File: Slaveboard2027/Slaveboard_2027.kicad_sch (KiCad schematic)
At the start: 137 parts, among them J1 Conn_01x01, J10 PB MB, J11 PA MA, J2 Conn_01x01, J3 Conn_01x01, J4 Conn_01x01, J5 Cells, J6 Temp, J7 Temp, J8 Temp, J9 Temp, Q1 DZTT5551, U1 LTC6812, U2 ADG728, U3 ADG728, U4 ADG728, U5 ADG728, U6 LTC6255, U7 LTC6255, U8 LTC6255, U9 LTC6255

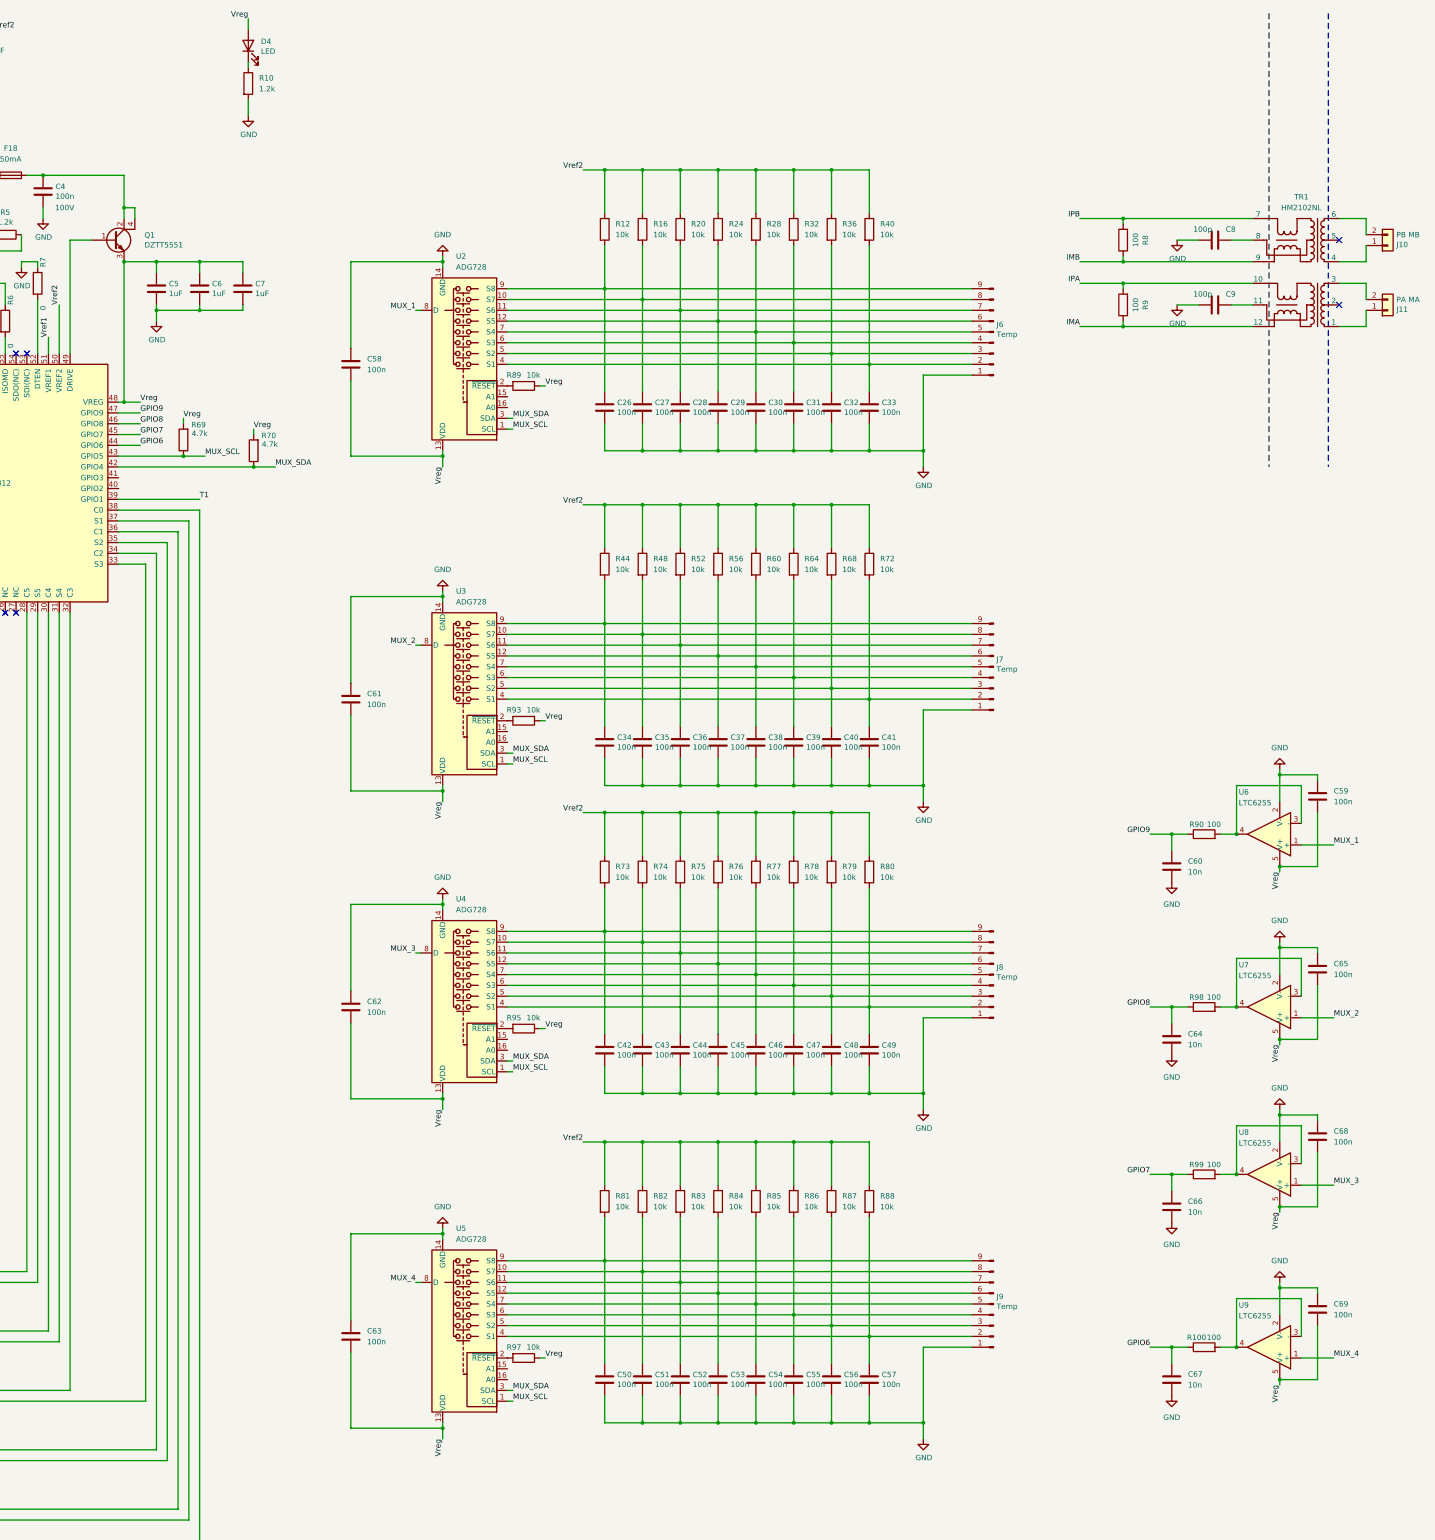
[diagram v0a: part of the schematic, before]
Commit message: Update slaveboard temperature multiplexer design
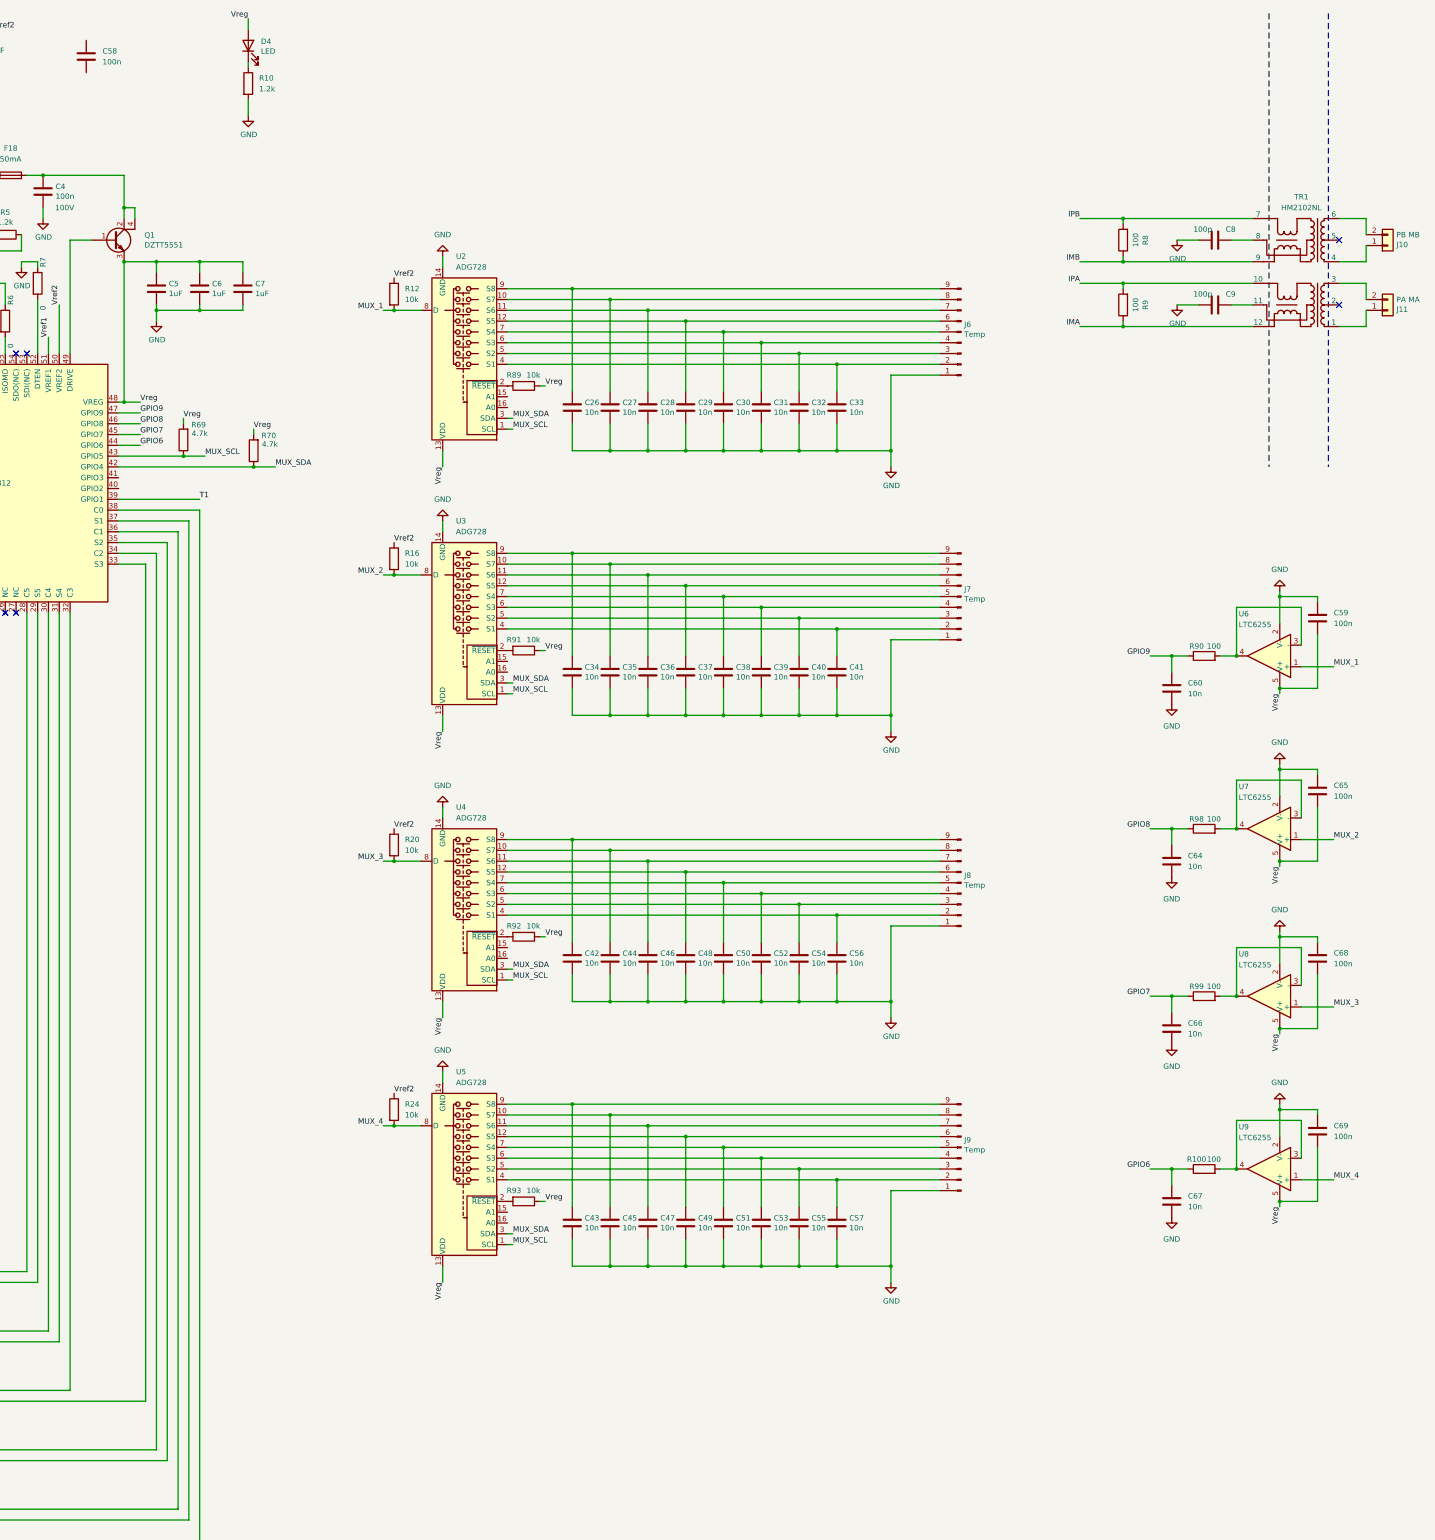
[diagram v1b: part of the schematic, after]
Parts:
- removed C61, C62, C63: 100n, Package_SO:TSSOP-16_4.4x5mm_P0.65mm, symbol Device:C
- removed R28, R32, R36, R40, R44, R48, R52, R56, R60, R64, R68, R72, R73, R74, R75, R76, R77, R78, R79, R80, R81, R82, R83, R84, R85, R86, R87, R88: 10k, Resistor_SMD:R_0603_1608Metric, symbol Device:R
- removed R95, R97: 10k, symbol Device:R
- added R91, R92: 10k, symbol Device:R
- C26, C27, C28, C29, C30, C31, C32, C33, C34, C35, C36, C37, C38, C39, C40, C41, C42, C43, C44, C45, C46, C47, C48, C49, C50, C51, C52, C53, C54, C55, C56, C57: value 100n -> 10n
- R12, R16, R20, R24: footprint Resistor_SMD:R_0603_1608Metric -> (none)
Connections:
- net GND: no longer C58.1
- net MUX_1: now also R12.2
- net MUX_2: now also R16.2
- net MUX_3: now also R20.2
- net MUX_4: now also R24.2
- net Vreg: now also R91.1, R92.1; no longer C58.2
- net at J9.6 (Pin_6), U5.12 (S5): now also C49.1; no longer C53.1
- net at U4.2 (~{RESET}): now also R92.2
- net at C28.1, J6.7 (Pin_7), U2.11 (S6): no longer R20.2
- net at J9.9 (Pin_9), U5.9 (S8): now also C43.1; no longer C50.1
- net at C27.1, J6.8 (Pin_8), U2.10 (S7): no longer R16.2
- net at J8.2 (Pin_2), U4.4 (S1): now also C56.1; no longer C49.1
- net at J8.8 (Pin_8), U4.10 (S7): now also C44.1; no longer C43.1
- net at C29.1, J6.6 (Pin_6), U2.12 (S5): no longer R24.2
- net at C26.1, J6.9 (Pin_9), U2.9 (S8): no longer R12.2
- net at J9.3 (Pin_3), U5.5 (S2): now also C55.1; no longer C56.1
- net at J9.7 (Pin_7), U5.11 (S6): now also C47.1; no longer C52.1
- net at J9.4 (Pin_4), U5.6 (S3): now also C53.1; no longer C55.1
- net at J8.4 (Pin_4), U4.6 (S3): now also C52.1; no longer C47.1
- net at J8.3 (Pin_3), U4.5 (S2): now also C54.1; no longer C48.1
- net at J9.8 (Pin_8), U5.10 (S7): now also C45.1; no longer C51.1
- net at J9.5 (Pin_5), U5.7 (S4): now also C51.1; no longer C54.1
- net at U5.2 (~{RESET}): now also R93.2
- net at J8.6 (Pin_6), U4.12 (S5): now also C48.1; no longer C45.1
- net at U3.2 (~{RESET}): now also R91.2; no longer R93.2
- net at J8.5 (Pin_5), U4.7 (S4): now also C50.1; no longer C46.1
- net at J8.7 (Pin_7), U4.11 (S6): now also C46.1; no longer C44.1
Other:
- moved on the sheet: C26, C27, C28, C29, C30, C31, C32, C33, C59, C60, C64, C65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
